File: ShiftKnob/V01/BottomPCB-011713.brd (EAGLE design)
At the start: 32.6 x 32.6 mm, 38 parts, among them IC2 7805DT, Q1 16MHz, Q2 MOSFET-NCHANNELSMD, Q3 MOSFET-NCHANNELSMD, Q4 MOSFET-NCHANNELSMD, Q5 MOSFET-NCHANNELSMD, Q6 MOSFET-NCHANNELSMD, U1 ATMEGA328

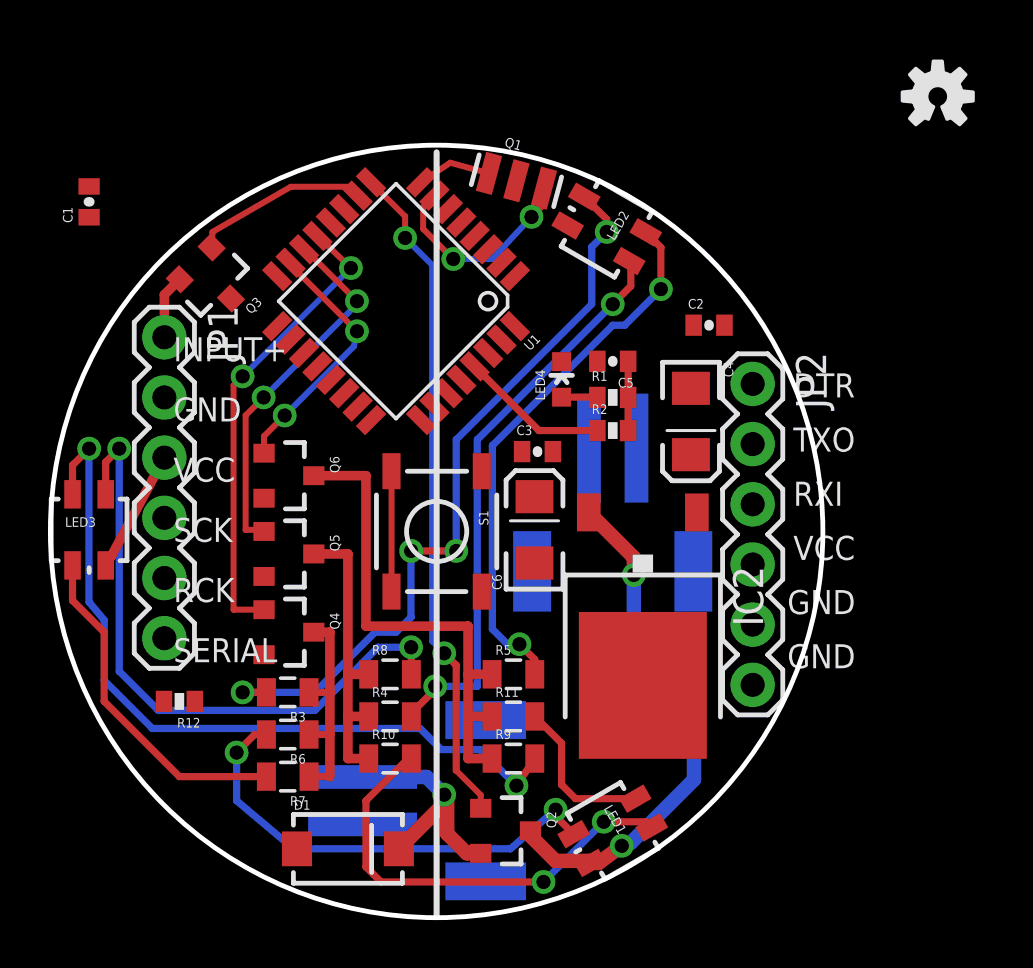
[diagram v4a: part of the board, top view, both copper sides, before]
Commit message: all traces done except ground.
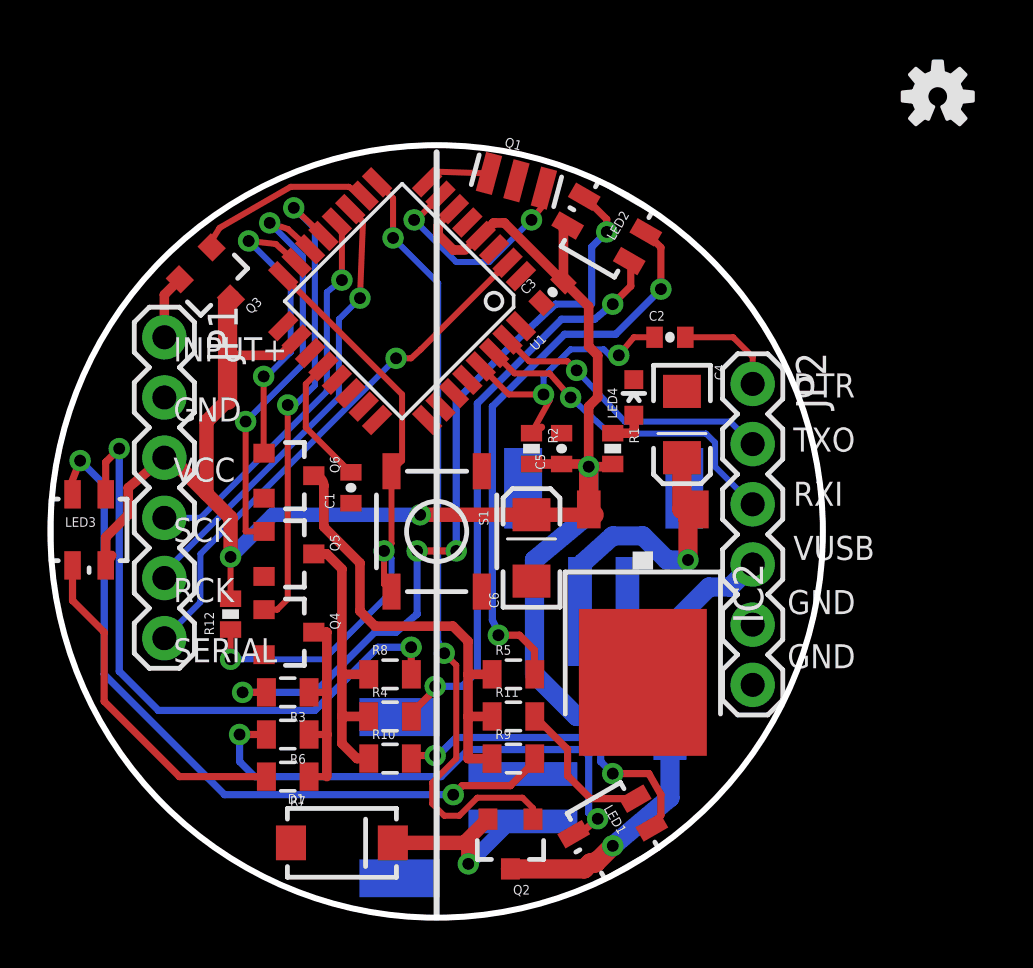
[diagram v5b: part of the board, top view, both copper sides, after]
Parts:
- added D2: MBR0520LT, diode:SOD123
- moved C1 16.4 mm to (16.4, 21.8)
- moved C3 6.76 mm to (24.9, 30.1), turned to 45 degrees
- moved R12 4.27 mm to (11.3, 16.5), turned to 90 degrees
- moved C5 4.27 mm to (25.3, 23.5), turned to 90 degrees
- moved R2 3.51 mm to (24.0, 23.5), turned to 270 degrees
- moved LED4 3.14 mm to (28.3, 25.7)
- moved R1 2.16 mm to (27.4, 23.5), turned to 270 degrees
- moved C2 1.73 mm to (29.8, 28.2)
- moved C6 0.77 mm to (24.0, 19.3)
- moved JP4 0.65 mm to (19.9, 8.76), turned to 270 degrees
- moved JP3 0.63 mm to (27.1, 20.3), turned to 0 degrees
- moved Q2 0.57 mm to (23.1, 6.86), turned to 180 degrees
- moved C4 0.40 mm to (30.4, 24.5)
- moved D1 0.36 mm to (16.0, 6.86)
- moved U1 0.25 mm to (18.5, 29.7)
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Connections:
- new net VUSB: D2.A, JP2.4
- net VCC: now also D2.C; no longer JP2.4
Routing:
- net VCC: track 30.2 -> 93.5 mm, vias 2 -> 4
- net D4/SERIAL: track 0.00 -> 22.4 mm, vias 0 -> 1
- net D12: track 5.08 -> 26.9 mm, vias 0 -> 2
- net D7/RCK: track 0.00 -> 19.2 mm, vias 0 -> 1
- net D8/SCK: track 0.00 -> 16.5 mm, vias 0 -> 1
- net RAW: track 0.00 -> 14.4 mm, vias 0 -> 1
- net RXI: track 0.00 -> 14.2 mm, vias 0 -> 1
- net TXO: track 0.00 -> 12.2 mm, vias 0 -> 1
- net VUSB: track 0.00 -> 5.72 mm
- net RESET: track 6.30 -> 12.0 mm, vias 0 -> 2
- net AREF: track 0.00 -> 5.57 mm
- net D5/MOTOR: track 28.3 -> 33.4 mm
- net N$7: track 18.9 -> 14.0 mm
- net DTR: track 0.00 -> 4.33 mm
- net N$9: track 19.8 -> 22.1 mm
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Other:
- board text added: "VUSB"

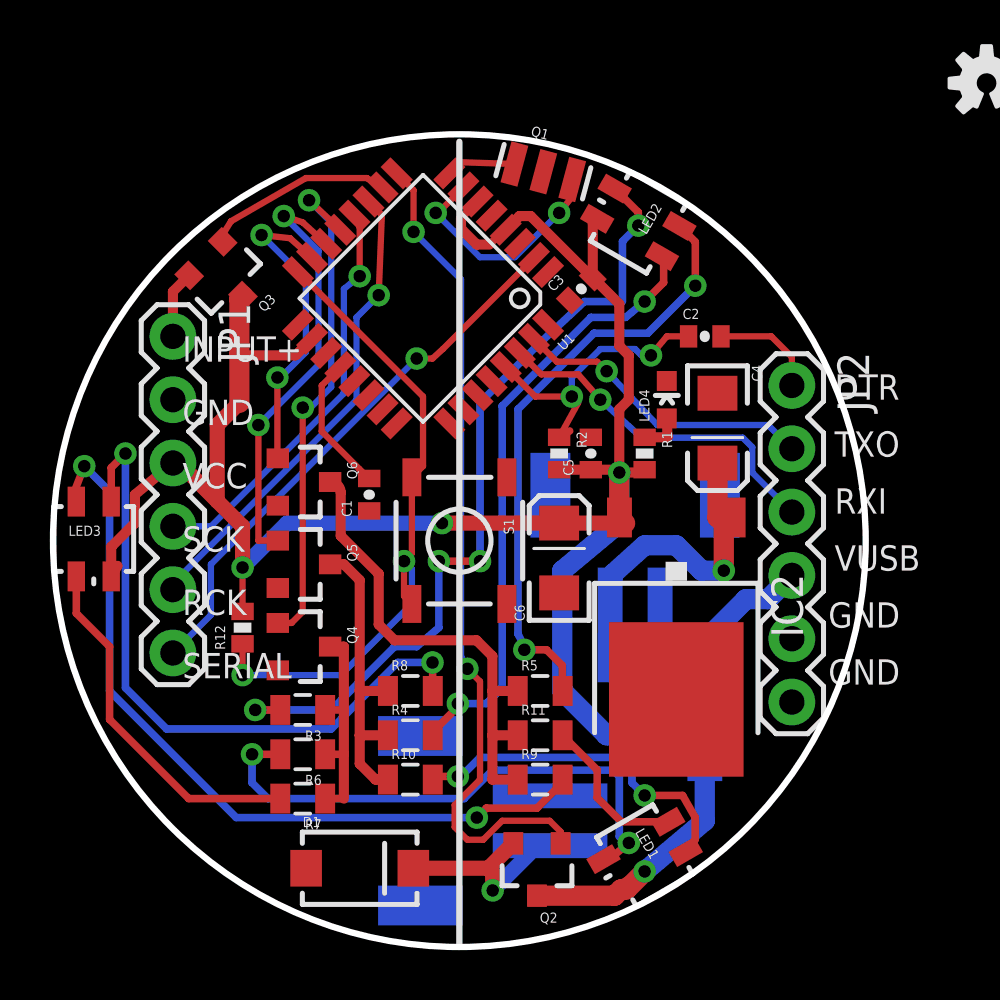
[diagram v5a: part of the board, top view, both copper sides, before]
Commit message: all traces complete. all GND pins connected and clear.
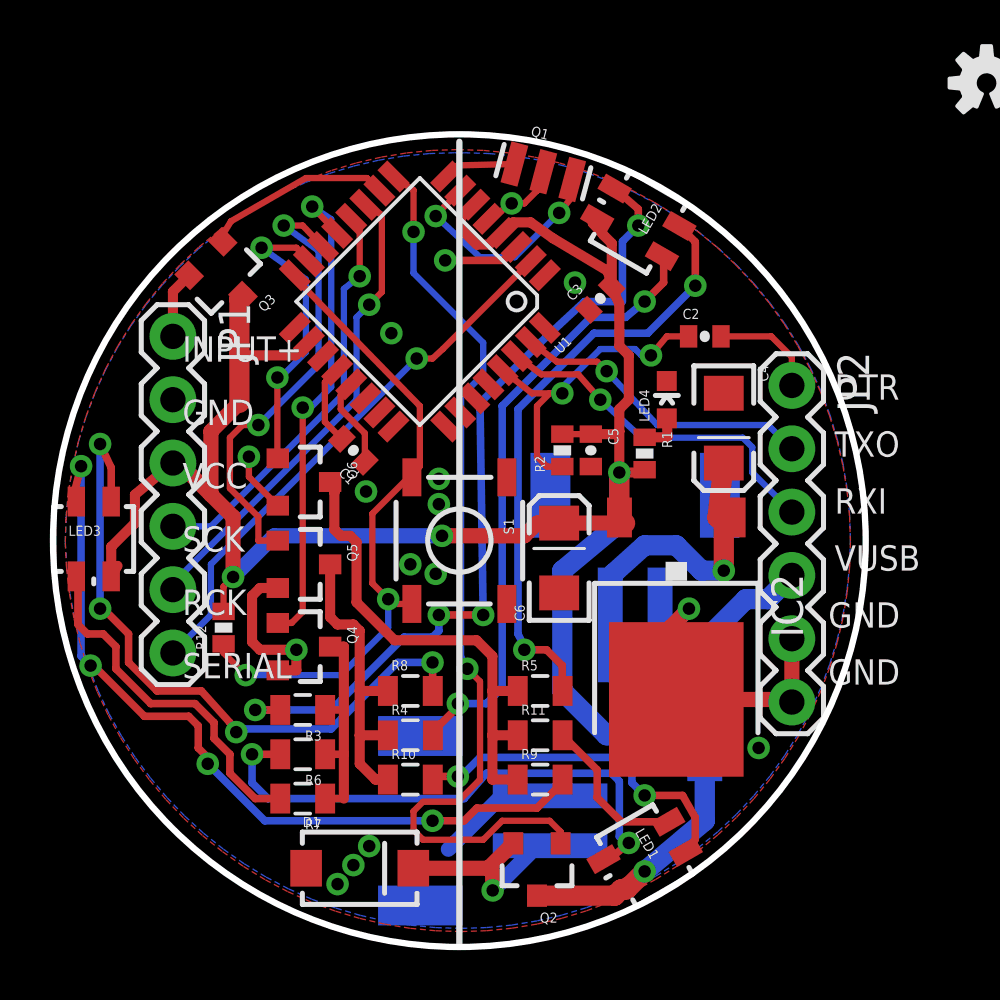
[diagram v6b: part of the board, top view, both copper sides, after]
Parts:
- moved C1 1.89 mm to (15.7, 23.6), turned to 135 degrees
- moved C3 0.85 mm to (25.7, 29.7)
- moved R12 0.76 mm to (10.5, 16.5)
- moved C4 0.25 mm to (30.6, 24.5)
- moved U1 0.18 mm to (18.4, 29.6)
- moved R2 0.18 mm to (24.1, 23.6), turned to 90 degrees
- moved C5 0.13 mm to (25.3, 23.6), turned to 270 degrees
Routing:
- net GND: track 0.00 -> 36.5 mm, vias 0 -> 16
- net D5/MOTOR: track 33.4 -> 37.4 mm
- net AREF: track 5.57 -> 3.24 mm
- net RESET: track 12.0 -> 13.2 mm
- net VCC: track 93.5 -> 94.5 mm
- net N$12: track 17.5 -> 18.4 mm
- net N$8: track 31.9 -> 32.5 mm, vias 2 -> 4
- net N$16: track 26.8 -> 27.4 mm, vias 2 -> 4
- net N$15: track 12.6 -> 12.0 mm
- net D12: track 26.9 -> 26.4 mm
- added copper zone on layer 1, net GND
- added copper zone on layer 16, net GND
